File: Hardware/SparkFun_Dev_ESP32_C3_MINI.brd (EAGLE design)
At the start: 17.8 x 33 mm, 44 parts, among them J1 USB Female Type C Connector, J5 Vertical Qwiic Connector, U1 ESP32-C3_MINI-1, U2 RT9080-33GJ5

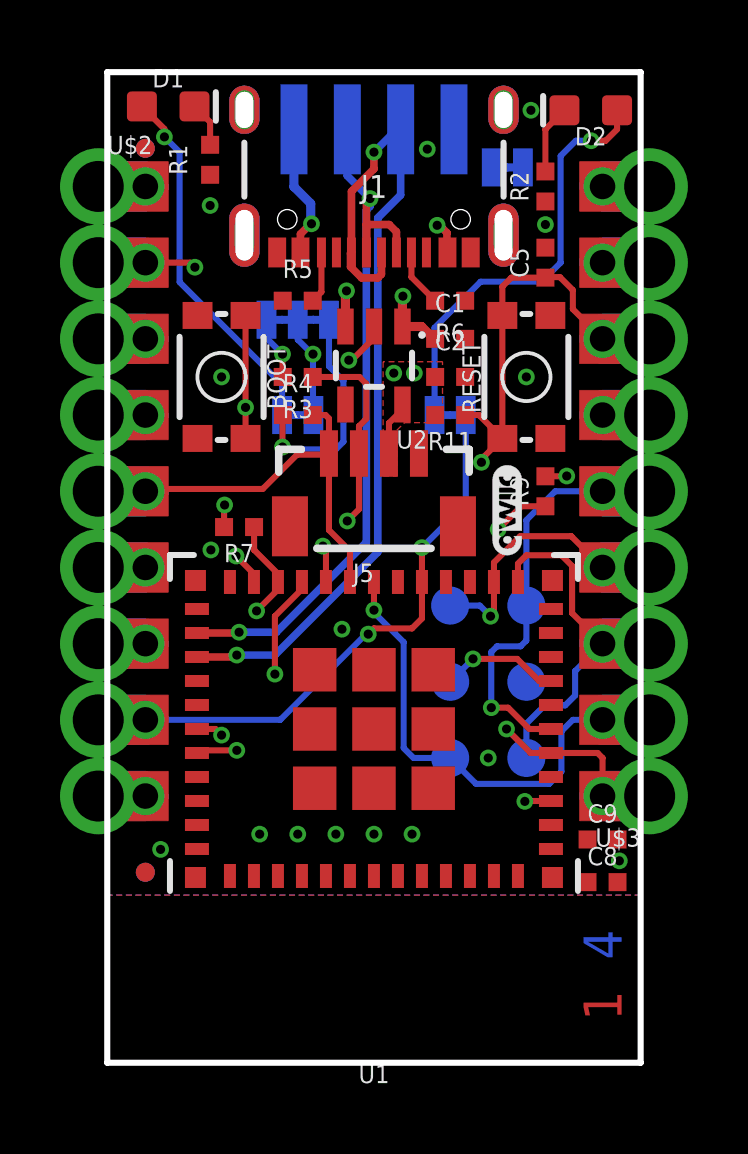
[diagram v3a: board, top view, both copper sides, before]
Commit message: Approves many many DRC errors generated by castellated leads
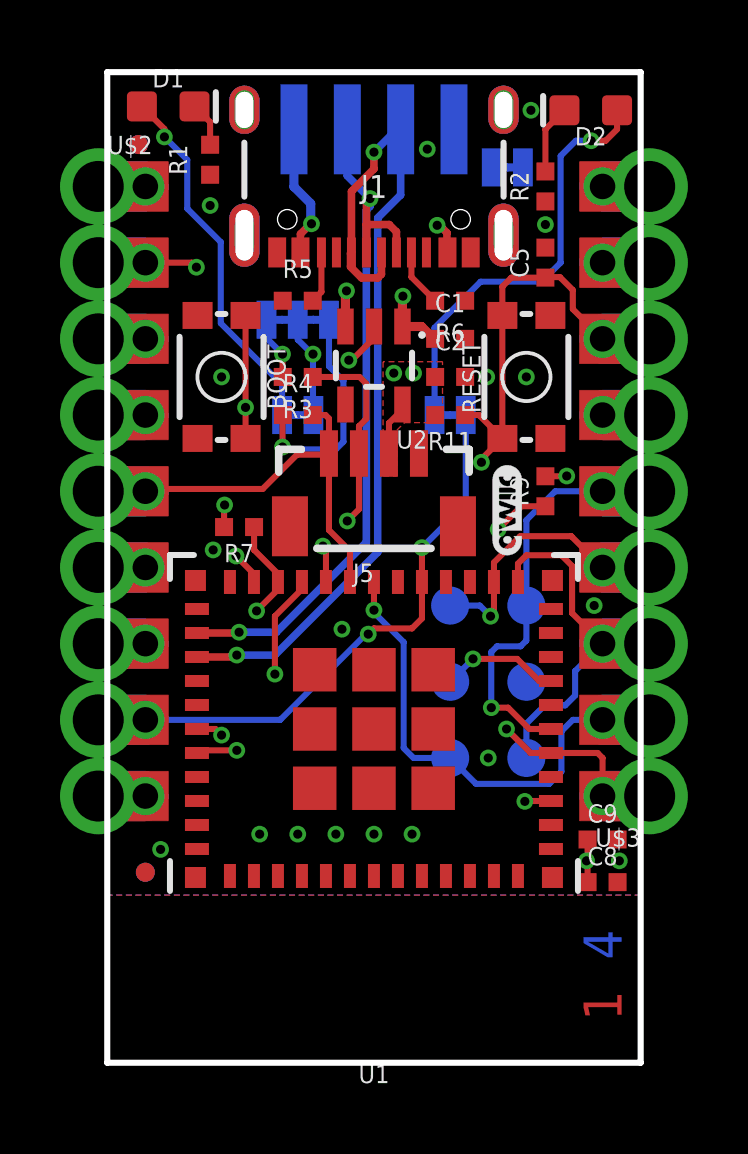
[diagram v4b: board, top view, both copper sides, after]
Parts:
- moved FD1 0.26 mm to (2.31, 30.6)
- moved FD2 0.26 mm to (2.31, 30.6)
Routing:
- net IO6/SDA/I2S_SDO: track 9.13 -> 15.7 mm
- net 3.3V: track 7.91 -> 13.0 mm, vias 6 -> 7
- net GND: vias 15 -> 18
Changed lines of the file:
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@@
 <setting verticaltext="up"/>
 </settings>
-<grid distance="0.01" unitdist="inch" unit="inch" style="dots" multiple="1" display="yes" altdistance="0.001" altunitdist="inch" altunit="inch"/>
+<grid distance="0.05" unitdist="inch" unit="inch" style="dots" multiple="1" display="yes" altdistance="0.001" altunitdist="inch" altunit="inch"/>
 <layers>
 <layer number="1" name="Top" color="4" fill="1" visible="yes" active="yes"/>
@@
 <layer number="20" name="Dimension" color="15" fill="1" visible="yes" active="yes"/>
 <layer number="21" name="tPlace" color="16" fill="1" visible="yes" active="yes"/>
-<layer number="22" name="bPlace" color="14" fill="1" visible="no" active="yes"/>
+<layer number="22" name="bPlace" color="14" fill="1" visible="yes" active="yes"/>
 <layer number="23" name="tOrigins" color="15" fill="1" visible="yes" active="yes"/>
 <layer number="24" name="bOrigins" color="15" fill="1" visible="yes" active="yes"/>
@@
 <layer number="27" name="tValues" color="7" fill="1" visible="no" active="yes"/>
 <layer number="28" name="bValues" color="7" fill="1" visible="no" active="yes"/>
-<layer number="29" name="tStop" color="7" fill="3" visible="yes" active="yes"/>
+<layer number="29" name="tStop" color="7" fill="3" visible="no" active="yes"/>
 <layer number="30" name="bStop" color="7" fill="6" visible="no" active="yes"/>
 <layer number="31" name="tCream" color="7" fill="4" visible="no" active="yes"/>
@@
 <layer number="37" name="tTest" color="7" fill="1" visible="no" active="yes"/>
 <layer number="38" name="bTest" color="7" fill="1" visible="no" active="yes"/>
-<layer number="39" name="tKeepout" color="4" fill="11" visible="yes" active="yes"/>
+<layer number="39" name="tKeepout" color="4" fill="11" visible="no" active="yes"/>
 <layer number="40" name="bKeepout" color="1" fill="11" visible="no" active="yes"/>
 <layer number="41" name="tRestrict" color="4" fill="10" visible="no" active="yes"/>
@@
 <layer number="47" name="Measures" color="7" fill="1" visible="no" active="yes"/>
 <layer number="48" name="Document" color="7" fill="1" visible="no" active="yes"/>
-<layer number="49" name="Reference" color="13" fill="1" visible="no" active="yes"/>
+<layer number="49" name="Reference" color="13" fill="1" visible="yes" active="yes"/>
 <layer number="50" name="dxf" color="7" fill="1" visible="no" active="no"/>
 <layer number="51" name="tDocu" color="6" fill="1" visible="yes" active="yes"/>
@@
 <element name="TP5" library="SparkFun-Connectors" package="PAD.03X.05" value="TEST-POINT3X5" x="12.7" y="12.7" smashed="yes" rot="MR0"/>
 <element name="TP6" library="SparkFun-Connectors" package="PAD.03X.05" value="TEST-POINT3X5" x="12.7" y="15.24" smashed="yes" rot="MR0"/>
-<element name="FD1" library="SparkFun-Aesthetics" package="FIDUCIAL-MICRO" value="FIDUCIALUFIDUCIAL" x="2.54" y="30.48" smashed="yes" rot="MR0"/>
-<element name="FD2" library="SparkFun-Aesthetics" package="FIDUCIAL-MICRO" value="FIDUCIALUFIDUCIAL" x="2.54" y="30.48" smashed="yes"/>
+<element name="FD1" library="SparkFun-Aesthetics" package="FIDUCIAL-MICRO" value="FIDUCIALUFIDUCIAL" x="2.3114" y="30.607" smashed="yes" rot="MR0"/>
+<element name="FD2" library="SparkFun-Aesthetics" package="FIDUCIAL-MICRO" value="FIDUCIALUFIDUCIAL" x="2.3114" y="30.607" smashed="yes"/>
 <element name="FD3" library="SparkFun-Aesthetics" package="FIDUCIAL-MICRO" value="FIDUCIALUFIDUCIAL" x="2.54" y="6.35" smashed="yes"/>
 <element name="FD4" library="SparkFun-Aesthetics" package="FIDUCIAL-MICRO" value="FIDUCIALUFIDUCIAL" x="2.54" y="6.35" smashed="yes" rot="MR0"/>
@@
 <vertex x="10.4648" y="23.368"/>
 </polygon>
-<via x="11.5062" y="22.987" extent="1-16" drill="0.3048"/>
+<via x="11.4808" y="22.987" extent="1-16" drill="0.3048"/>
 <wire x1="15.875" y1="19.55" x2="16.5782" y2="19.55" width="0.2032" layer="1"/>
 <wire x1="16.5782" y1="19.55" x2="16.5862" y2="19.558" width="0.2032" layer="1"/>
@@
 <wire x1="8.128" y1="23.622" x2="8.1026" y2="23.622" width="0.2032" layer="16"/>
 <via x="10.8204" y="22.987" extent="1-16" drill="0.3048"/>
-<wire x1="17.28" y1="7.4422" x2="17.28" y2="6.0198" width="0" layer="19" extent="1-1"/>
-<wire x1="16.06" y1="8.7252" x2="17.28" y2="7.4422" width="0" layer="19" extent="1-1"/>
+<wire x1="15.8242" y1="6.731" x2="15.1892" y2="7.366" width="0.2032" layer="2"/>
+<wire x1="15.1892" y1="8.7122" x2="15.1892" y2="7.366" width="0.2032" layer="2"/>
+<wire x1="15.8242" y1="6.731" x2="17.2466" y2="6.731" width="0.2032" layer="2"/>
+<via x="17.2466" y="6.731" extent="1-16" drill="0.3048"/>
+<wire x1="17.28" y1="7.4422" x2="17.28" y2="6.7644" width="0.2032" layer="1"/>
+<wire x1="17.28" y1="6.7644" x2="17.2466" y2="6.731" width="0.2032" layer="1"/>
+<wire x1="17.28" y1="6.0198" x2="17.28" y2="6.7644" width="0.2032" layer="1"/>
 </signal>
 <signal name="GND">
@@
 <wire x1="9.4234" y1="23.4188" x2="9.3218" y2="23.4188" width="0.2032" layer="1"/>
 <via x="9.3218" y="23.4188" extent="1-16" drill="0.3048"/>
-<via x="4.7244" y="17.0942" extent="1-16" drill="0.3048"/>
+<via x="4.8006" y="17.0942" extent="1-16" drill="0.3048"/>
 <via x="5.08" y="22.86" extent="1-16" drill="0.3048"/>
 <via x="15.24" y="22.86" extent="1-16" drill="0.3048"/>
@@
 <via x="11.938" y="30.4546" extent="1-16" drill="0.3048"/>
 <via x="18.3388" y="6.731" extent="1-16" drill="0.3048"/>
-<wire x1="13.2" y1="22.86" x2="15.24" y2="22.86" width="0" layer="19" extent="1-1"/>
-<wire x1="15.24" y1="12.7" x2="16.06" y2="15.1252" width="0" layer="19" extent="1-16"/>
+<via x="17.5006" y="15.24" extent="1-16" drill="0.3048"/>
+<via x="13.9192" y="22.86" extent="1-16" drill="0.3048"/>
+<via x="13.97" y="10.16" extent="1-16" drill="0.3048"/>
 </signal>
 <signal name="N$4">
@@
 <contactref element="PWR" pad="1"/>
 <wire x1="7.0993" y1="21.59" x2="7.0993" y2="22.606" width="0.2032" layer="16"/>
-<wire x1="7.0993" y1="22.606" x2="3.683" y2="26.0223" width="0.2032" layer="16"/>
-<wire x1="3.683" y1="30.353" x2="3.175" y2="30.861" width="0.2032" layer="16"/>
+<wire x1="7.0993" y1="22.606" x2="5.0546" y2="24.6507" width="0.2032" layer="16"/>
+<wire x1="5.0546" y1="27.3558" x2="3.937" y2="28.4734" width="0.2032" layer="16"/>
+<wire x1="3.937" y1="30.099" x2="3.175" y2="30.861" width="0.2032" layer="16"/>
+<wire x1="3.937" y1="30.099" x2="3.937" y2="28.4734" width="0.2032" layer="16"/>
 <via x="3.175" y="30.861" extent="1-16" drill="0.3048"/>
 <wire x1="3.175" y1="30.861" x2="3.175" y2="31.127" width="0.2032" layer="1"/>
 <wire x1="3.175" y1="31.127" x2="2.425" y2="31.877" width="0.2032" layer="1"/>
-<wire x1="3.683" y1="26.0223" x2="3.683" y2="30.353" width="0.2032" layer="16"/>
+<wire x1="5.0546" y1="24.6507" x2="5.0546" y2="27.3558" width="0.2032" layer="16"/>
 </signal>
 <signal name="IO21/RXI">
@@
 <via x="5.588" y="10.414" extent="1-16" drill="0.3048"/>
 <wire x1="5.588" y1="10.414" x2="5.588" y2="12.6746" width="0.2032" layer="15"/>
-<wire x1="4.191" y1="14.0716" x2="4.191" y2="26.5176" width="0.2032" layer="15"/>
-<via x="4.191" y="26.5176" extent="1-16" drill="0.3048"/>
-<wire x1="5.588" y1="12.6746" x2="4.191" y2="14.0716" width="0.2032" layer="15"/>
-<wire x1="2.54" y1="26.67" x2="4.0386" y2="26.67" width="0.2032" layer="1"/>
-<wire x1="4.0386" y1="26.67" x2="4.191" y2="26.5176" width="0.2032" layer="1"/>
+<wire x1="4.2418" y1="14.0208" x2="4.2418" y2="26.5176" width="0.2032" layer="15"/>
+<via x="4.2418" y="26.5176" extent="1-16" drill="0.3048"/>
+<wire x1="5.588" y1="12.6746" x2="4.2418" y2="14.0208" width="0.2032" layer="15"/>
+<wire x1="2.54" y1="26.67" x2="4.0894" y2="26.67" width="0.2032" layer="1"/>
+<wire x1="4.0894" y1="26.67" x2="4.2418" y2="26.5176" width="0.2032" layer="1"/>
 <wire x1="2.54" y1="26.67" x2="0.97" y2="26.67" width="0" layer="19" extent="1-1"/>
 </signal>
@@
 <wire x1="8.56" y1="16.0252" x2="8.56" y2="17.1194" width="0.2032" layer="1"/>
 <wire x1="8.56" y1="17.1194" x2="8.4582" y2="17.2212" width="0.2032" layer="1"/>
-<wire x1="2.54" y1="16.51" x2="8.4582" y2="17.2212" width="0" layer="19" extent="1-1"/>
+<wire x1="8.4582" y1="17.2212" x2="7.366" y2="16.129" width="0.2032" layer="2"/>
+<wire x1="2.921" y1="16.129" x2="2.54" y2="16.51" width="0.2032" layer="2"/>
+<wire x1="7.366" y1="16.129" x2="2.921" y2="16.129" width="0.2032" layer="2"/>
 <wire x1="0.97" y1="16.51" x2="2.54" y2="16.51" width="0" layer="19" extent="1-1"/>
 </signal>
@@
 <wire x1="0.97" y1="13.97" x2="2.54" y2="13.97" width="0" layer="19" extent="1-1"/>
 </signal>
-<signal name="N$16">
-<via x="13.97" y="10.16" extent="1-16" drill="0.3048"/>
-</signal>
 <signal name="N$20">

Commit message: Renames some nets for clarity, adds vias, cleans up  ground pours, fixes air wires
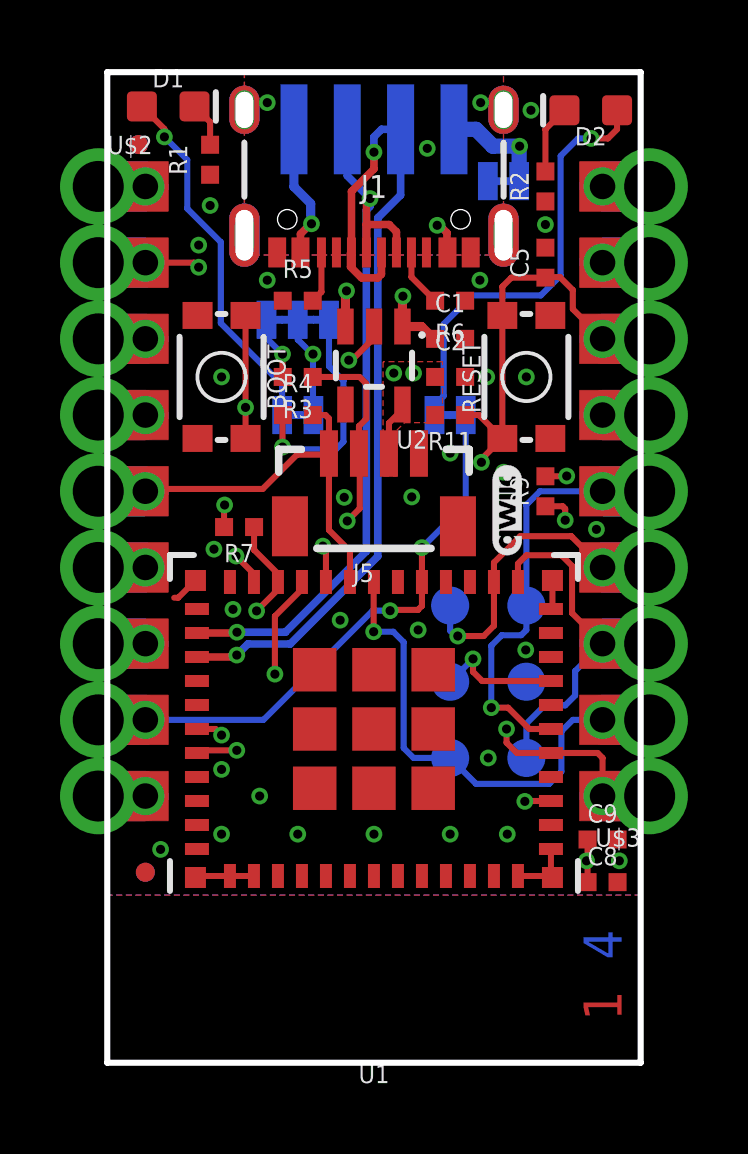
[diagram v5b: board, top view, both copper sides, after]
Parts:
- moved SHLD 0.47 mm to (14.5, 29.4)
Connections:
- net IO10/I2S_WS renamed IO10/I2S_FS
- net IO5/SCL/BCK renamed IO5/SCL/I2S_SCK
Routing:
- net GND: track 1.53 -> 11.1 mm, vias 18 -> 21
- net IOA2: track 13.5 -> 14.9 mm
- net IOA1/POCI/MTDI: track 7.75 -> 9.04 mm
- added copper zone on layer 1, net SHLD
- added copper zone on layer 15, net SHLD
- added copper zone on layer 16, net SHLD
- added copper zone on layer 2, net SHLD

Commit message: Adds most of the silk on the bottom side
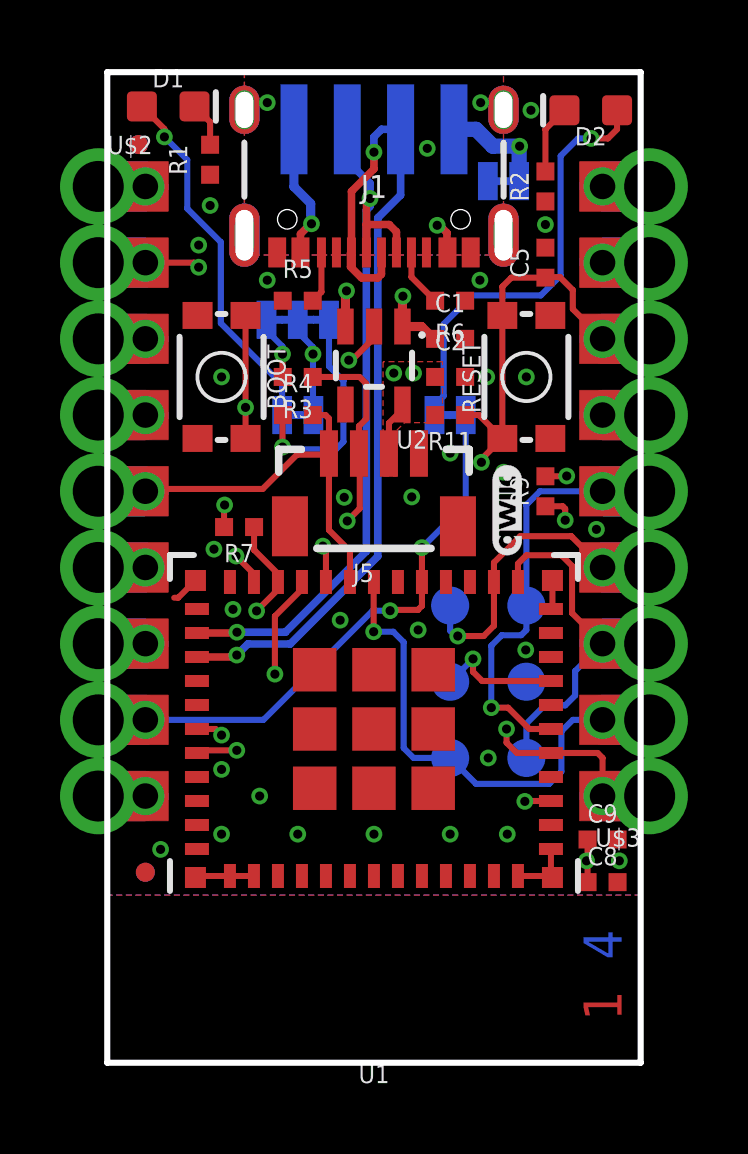
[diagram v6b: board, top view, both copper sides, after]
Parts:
- added U$1, U$4: (no value), bot:#GND#4
- added U$10: (no value), bot:#RXI#11
- added U$11: (no value), bot:#TXO#12
- added U$12: (no value), bot:#3V3#0
- added U$13: (no value), prod:#A3#PICO#35
- added U$14: (no value), prod:#A1#POCI#35
- added U$15: (no value), prod:#A2#35
- added U$16: (no value), prod:#A0#SCLK#35
- added U$17: (no value), prod:#A4#35
- added U$18: (no value), prod:#8#35
- added U$19: (no value), prod:#10#FS#35
- added U$20: (no value), prod:#7#SDI#35
- added U$21: (no value), prod:#6#SDA#SDO#35
- added U$22: (no value), prod:#5#SCL#SCK#35
- added U$5: (no value), prod:#EN#34
- added U$6: (no value), bot:#I2C#16
- added U$7: (no value), bot:#STAT#15
- added U$8: (no value), bot:#PWR#14
- added U$9: (no value), top:#SHLD#14
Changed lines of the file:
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@@
 <setting verticaltext="up"/>
 </settings>
-<grid distance="0.01" unitdist="inch" unit="inch" style="dots" multiple="1" display="yes" altdistance="0.001" altunitdist="inch" altunit="inch"/>
+<grid distance="0.5" unitdist="mm" unit="mm" style="dots" multiple="1" display="yes" altdistance="0.01" altunitdist="mm" altunit="mm"/>
 <layers>
 <layer number="1" name="Top" color="4" fill="1" visible="yes" active="yes"/>
-<layer number="2" name="Route2" color="23" fill="1" visible="yes" active="yes"/>
-<layer number="15" name="Route15" color="10" fill="1" visible="yes" active="yes"/>
+<layer number="2" name="Route2" color="23" fill="1" visible="no" active="yes"/>
+<layer number="15" name="Route15" color="10" fill="1" visible="no" active="yes"/>
 <layer number="16" name="Bottom" color="3" fill="1" visible="yes" active="yes"/>
 <layer number="17" name="Pads" color="26" fill="1" visible="yes" active="yes"/>
@@
 <attribute name="VALUE" x="10.16" y="17.6252" size="0.6096" layer="27" font="vector" ratio="20" rot="R180" align="center"/>
 </element>
+<element name="U$1" library="bot" package="#GND#4" value="" x="15.748" y="26.289" smashed="yes" rot="MR0"/>
+<element name="U$4" library="bot" package="#GND#4" value="" x="3.429" y="22.86" smashed="yes" rot="MR270"/>
+<element name="U$6" library="bot" package="#I2C#16" value="" x="8.128" y="26.289" smashed="yes" rot="MR0"/>
+<element name="U$7" library="bot" package="#STAT#15" value="" x="12.573" y="20.066" smashed="yes" rot="MR0"/>
+<element name="U$8" library="bot" package="#PWR#14" value="" x="7.62" y="20.066" smashed="yes" rot="MR0"/>
+<element name="U$9" library="top" package="#SHLD#14" value="" x="11.557" y="29.337" smashed="yes" rot="MR0"/>
+<element name="U$10" library="bot" package="#RXI#11" value="" x="4.318" y="29.21" smashed="yes" rot="MR0"/>
+<element name="U$11" library="bot" package="#TXO#12" value="" x="4.572" y="26.67" smashed="yes" rot="MR0"/>
+<element name="U$5" library="prod" package="#EN#34" value="" x="16.256" y="24.13" smashed="yes" rot="MR0"/>
+<element name="U$12" library="bot" package="#3V3#0" value="" x="15.875" y="21.59" smashed="yes" rot="MR0"/>
+<element name="U$13" library="prod" package="#A3#PICO#35" value="" x="14.54" y="19.01" smashed="yes" rot="MR0"/>
+<element name="U$14" library="prod" package="#A1#POCI#35" value="" x="14.66" y="16.48" smashed="yes" rot="MR0"/>
+<element name="U$15" library="prod" package="#A2#35" value="" x="16.19" y="8.88" smashed="yes" rot="MR0"/>
+<element name="U$16" library="prod" package="#A0#SCLK#35" value="" x="14.46" y="13.95" smashed="yes" rot="MR0"/>
+<element name="U$17" library="prod" package="#A4#35" value="" x="16.2" y="11.44" smashed="yes" rot="MR0"/>
+<element name="U$18" library="prod" package="#8#35" value="" x="3.66" y="8.82" smashed="yes" rot="MR0"/>
+<element name="U$19" library="prod" package="#10#FS#35" value="" x="4.92" y="11.44" smashed="yes" rot="MR0"/>
+<element name="U$20" library="prod" package="#7#SDI#35" value="" x="4.82" y="13.88" smashed="yes" rot="MR0"/>
+<element name="U$21" library="prod" package="#6#SDA#SDO#35" value="" x="6.52" y="16.5" smashed="yes" rot="MR0"/>
+<element name="U$22" library="prod" package="#5#SCL#SCK#35" value="" x="6.42" y="18.99" smashed="yes" rot="MR0"/>
 </elements>
 <signals>
@@
 <wire x1="9.91" y1="27.01" x2="9.91" y2="27.936" width="0.254" layer="1"/>
 <wire x1="9.91" y1="27.936" x2="9.906" y2="27.94" width="0.254" layer="1"/>
-<wire x1="9.271" y1="31.115" x2="9.271" y2="29.5656" width="0.254" layer="16"/>
+<wire x1="9.271" y1="31.115" x2="9.271" y2="30.0736" width="0.254" layer="16"/>
 <via x="10.029171875" y="28.807428125" extent="1-16" drill="0.3048"/>
-<wire x1="9.271" y1="29.5656" x2="10.029171875" y2="28.807428125" width="0.254" layer="16"/>
+<wire x1="10.029171875" y1="29.315428125" x2="10.029171875" y2="28.807428125" width="0.254" layer="16"/>
+<wire x1="10.029171875" y1="29.315428125" x2="9.271" y2="30.0736" width="0.254" layer="16"/>
 <wire x1="9.91" y1="27.01" x2="9.91" y2="28.68825625" width="0.254" layer="1"/>
 <wire x1="9.91" y1="28.68825625" x2="10.029171875" y2="28.807428125" width="0.254" layer="1"/>
@@
 <wire x1="8.128" y1="21.6027" x2="8.128" y2="23.622" width="0.2032" layer="16"/>
 <via x="8.128" y="23.622" extent="1-16" drill="0.3048"/>
-<wire x1="8.1026" y1="23.622" x2="7.62" y2="24.1046" width="0.2032" layer="16"/>
-<wire x1="7.62" y1="24.765" x2="7.62" y2="24.1046" width="0.2032" layer="16"/>
-<wire x1="8.128" y1="23.622" x2="8.1026" y2="23.622" width="0.2032" layer="16"/>
+<wire x1="8.128" y1="23.622" x2="8.128" y2="23.8506" width="0.2032" layer="16"/>
+<wire x1="8.128" y1="23.8506" x2="7.62" y2="24.3586" width="0.2032" layer="16"/>
+<wire x1="7.62" y1="24.765" x2="7.62" y2="24.3586" width="0.2032" layer="16"/>
 <via x="10.8204" y="22.987" extent="1-16" drill="0.3048"/>
 <wire x1="15.8242" y1="6.731" x2="15.1892" y2="7.366" width="0.2032" layer="2"/>
@@
 <wire x1="7.112" y1="22.868" x2="7.112" y2="23.622" width="0.2032" layer="1"/>
 <via x="7.112" y="23.622" extent="1-16" drill="0.3048"/>
-<wire x1="7.112" y1="23.622" x2="6.5786" y2="24.1554" width="0.2032" layer="16"/>
-<wire x1="6.5786" y1="24.1554" x2="6.5786" y2="24.765" width="0.2032" layer="16"/>
+<wire x1="7.112" y1="23.622" x2="7.112" y2="23.876" width="0.2032" layer="16"/>
+<wire x1="7.112" y1="23.876" x2="6.5786" y2="24.4094" width="0.2032" layer="16"/>
+<wire x1="6.5786" y1="24.4094" x2="6.5786" y2="24.765" width="0.2032" layer="16"/>
 </signal>
 <signal name="N$5">
